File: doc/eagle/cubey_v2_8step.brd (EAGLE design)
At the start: 72.6 x 56 mm, 33 parts, among them K1 PIN20X2

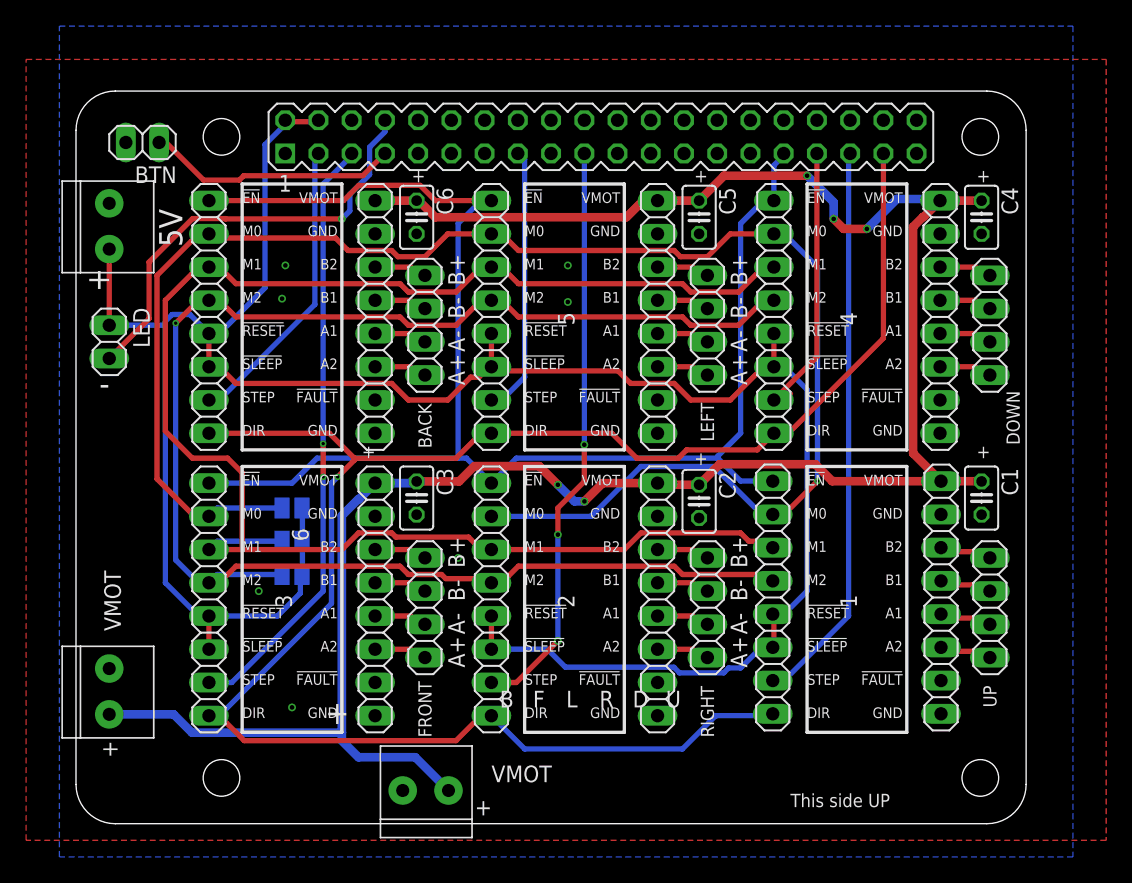
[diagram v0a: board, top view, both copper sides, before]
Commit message: Added links to Fusion 360 CAD files, updated Cubey PCB EAGLE files.
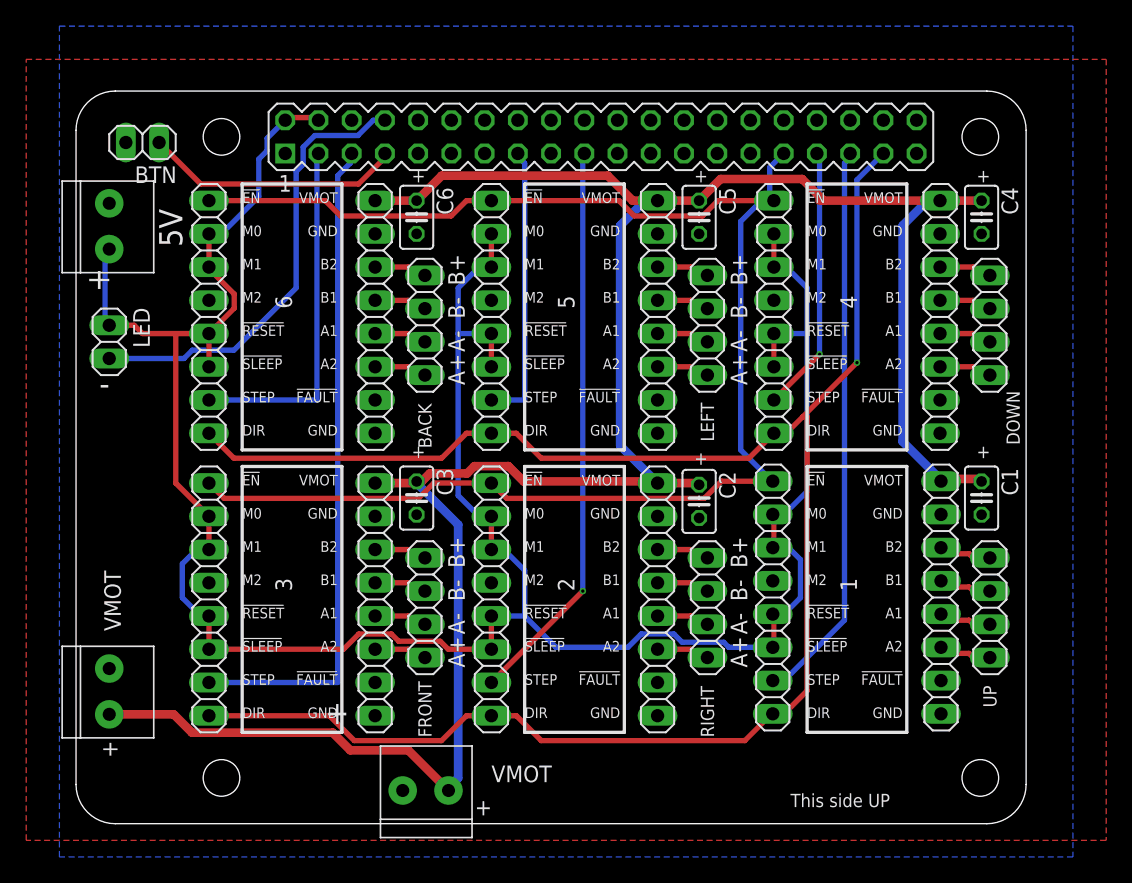
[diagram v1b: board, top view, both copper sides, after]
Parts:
- removed SJ1, SJ2, SJ3: (no value), jumper:SJ
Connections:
- removed net MODE0: JP1.2, JP11.2, JP3.2, JP5.2, JP7.2, JP9.2, SJ1.2
- removed net MODE1: JP1.3, JP11.3, JP3.3, JP5.3, JP7.3, JP9.3, SJ2.2
- removed net MODE2: JP1.4, JP11.4, JP3.4, JP5.4, JP7.4, JP9.4, SJ3.2
- net +5V: now also JP1.2, JP1.3, JP11.2, JP11.3, JP3.2, JP3.3, JP5.2, JP5.3, JP7.2, JP7.3, JP9.2, JP9.3; no longer SJ1.1, SJ2.1, SJ3.1
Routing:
- net MODE0: track 127.7 -> 0.00 mm, vias 1 -> 0
- net MODE1: track 124.8 -> 0.00 mm
- net MODE2: track 121.9 -> 0.00 mm, vias 1 -> 0
- net +5V: track 184.0 -> 199.4 mm
- net VCC: track 173.5 -> 182.1 mm, vias 5 -> 0
- net FRONT: track 46.0 -> 50.7 mm, vias 2 -> 0
- net BACK: track 22.8 -> 27.1 mm
- net !EN_MOT: track 115.8 -> 118.6 mm
- net DOWN: track 21.8 -> 20.4 mm, vias 0 -> 1
- net RIGHT: track 44.5 -> 43.4 mm, vias 3 -> 1
- net !LED: track 33.7 -> 34.6 mm, vias 1 -> 0
- net LEFT: track 20.7 -> 21.6 mm
- net DIR: track 143.6 -> 142.7 mm
- net BTN: track 19.3 -> 19.9 mm
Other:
- board text removed: "B"
- board text removed: "D"
- board text removed: "F"
- board text removed: "L"
- board text removed: "R"
- board text removed: "U"
